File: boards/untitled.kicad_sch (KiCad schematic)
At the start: 20 parts, among them J11 RE12A, J12 RS485_airdata, Q3 NPN, U8 MAX3485, U9 MOUDLE-SEEEDUINO-XIAO-ESP32C3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

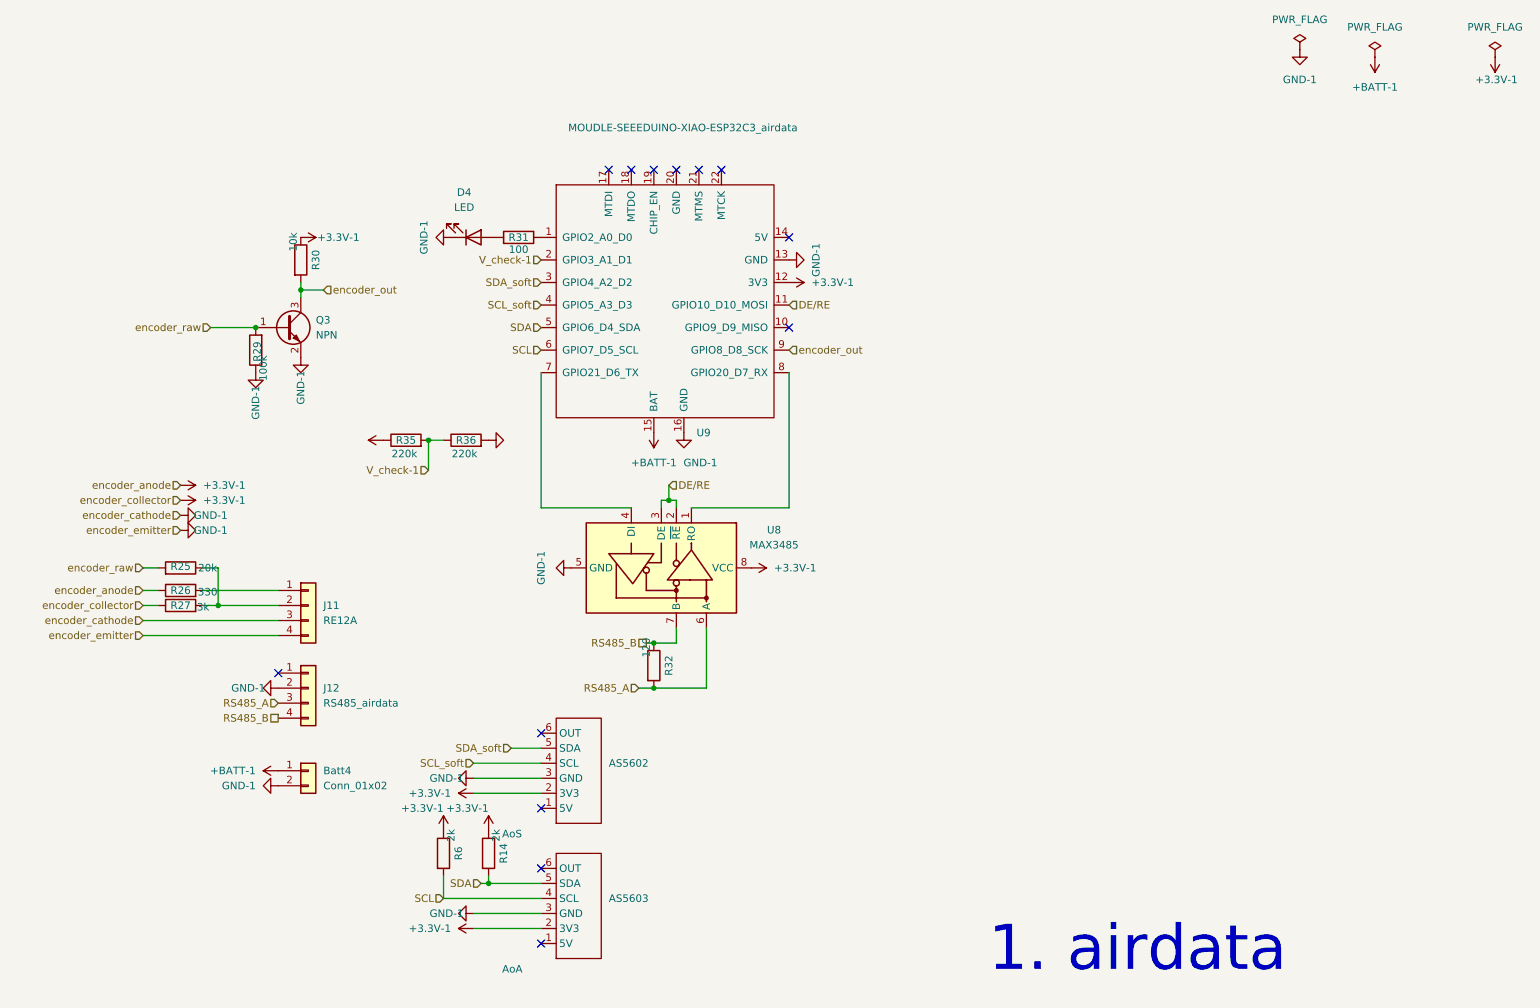
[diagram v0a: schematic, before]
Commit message: 増幅回路追加
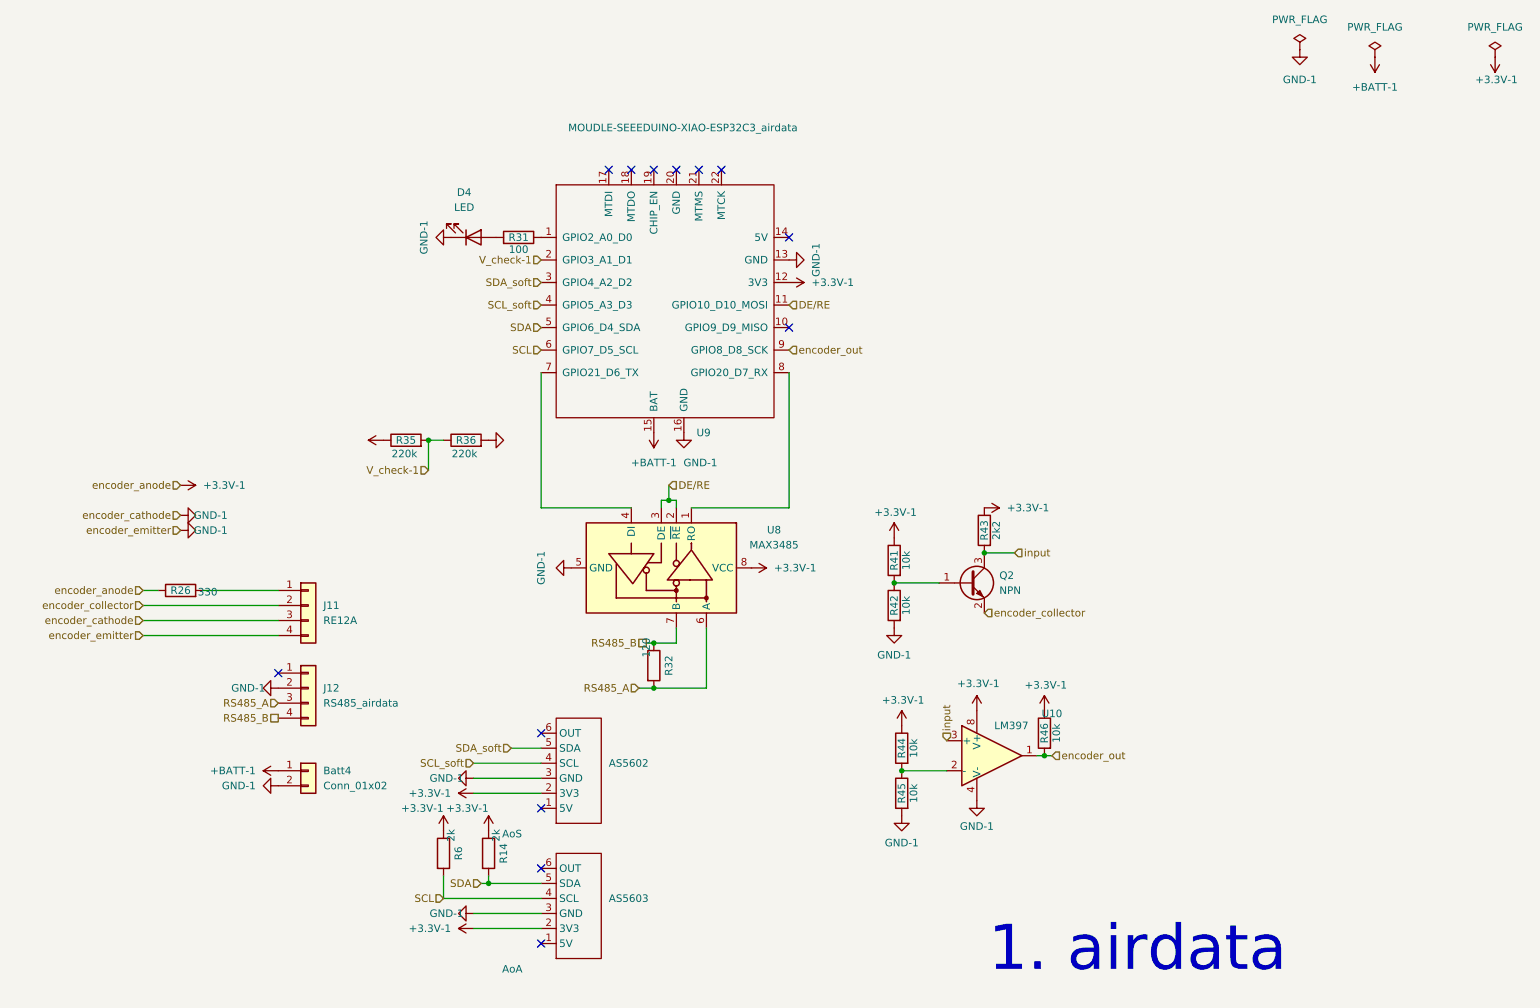
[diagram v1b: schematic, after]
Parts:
- removed Q3: NPN, Package_TO_SOT_SMD:SOT-23, symbol Transistor_BJT:MMBT2222A
- removed R25: 20k, Resistor_SMD:R_0603_1608Metric_Pad0.98x0.95mm_HandSolder, symbol Device:R
- removed R27: 3k, Resistor_SMD:R_0603_1608Metric_Pad0.98x0.95mm_HandSolder, symbol Device:R
- removed R29: 100k, Resistor_SMD:R_0603_1608Metric_Pad0.98x0.95mm_HandSolder, symbol Device:R
- removed R30: 10k, Resistor_SMD:R_0603_1608Metric_Pad0.98x0.95mm_HandSolder, symbol Device:R
- added Q2: NPN, Package_TO_SOT_SMD:SOT-23, symbol Transistor_BJT:MMBT2222A
- added R41, R42, R44, R45, R46: 10k, Resistor_SMD:R_0603_1608Metric_Pad0.98x0.95mm_HandSolder, symbol Device:R
- added R43: 2k2, Resistor_SMD:R_0603_1608Metric_Pad0.98x0.95mm_HandSolder, symbol Device:R
- added U10: LM397, Package_SO:SOP-8_3.9x4.9mm_P1.27mm, symbol Comparator:LM397
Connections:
- net +3.3V-1: now also R41.1, R43.1, R44.1, R46.1, U10.8 (V+)
- net GND-1: now also R42.2, R45.2, U10.4 (V-)
- net encoder_out: now also R46.2, U10.1
- net encoder_collector: now reaches J11.2 (Pin_2)
- net encoder_collector: now also Q2.2 (E)
- new net: Q2.1 (B), R41.2, R42.1
- new net: R44.2, R45.1, U10.2 (-)
- new net input: Q2.3 (C), R43.2, U10.3 (+)

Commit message: DRCエラー解消
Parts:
- R26: value 330 -> 150
- U10: value LM397 -> TJ393
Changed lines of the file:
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@@
 			)
 		)
-		(property "Value" "LM397"
+		(property "Value" "TJ393"
 			(at 189.992 135.89 0)
 			(effects
@@
 			)
 		)
-		(property "Value" "330"
+		(property "Value" "150"
 			(at 54.102 113.284 90)
 			(effects

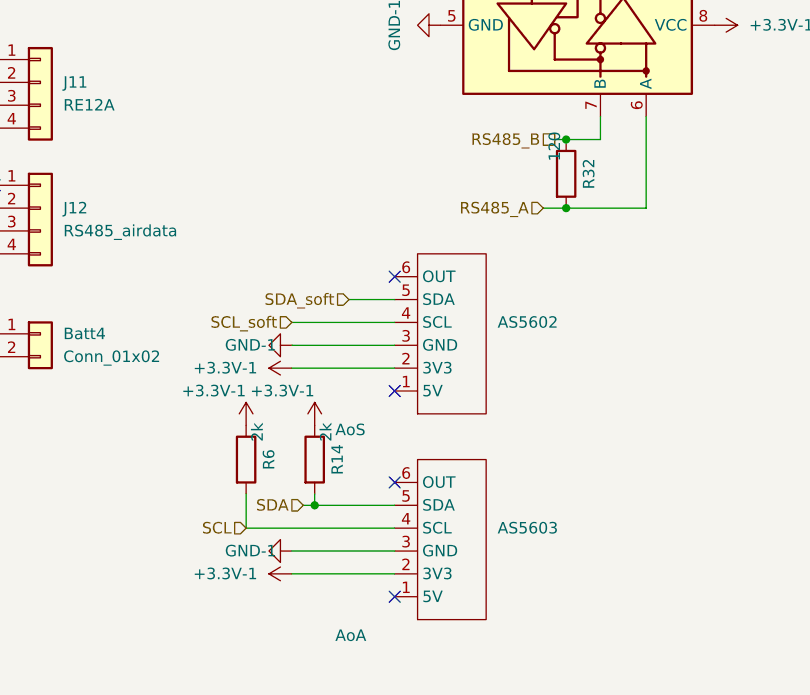
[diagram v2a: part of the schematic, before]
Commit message: 動作確認をもとに統合版コード修正
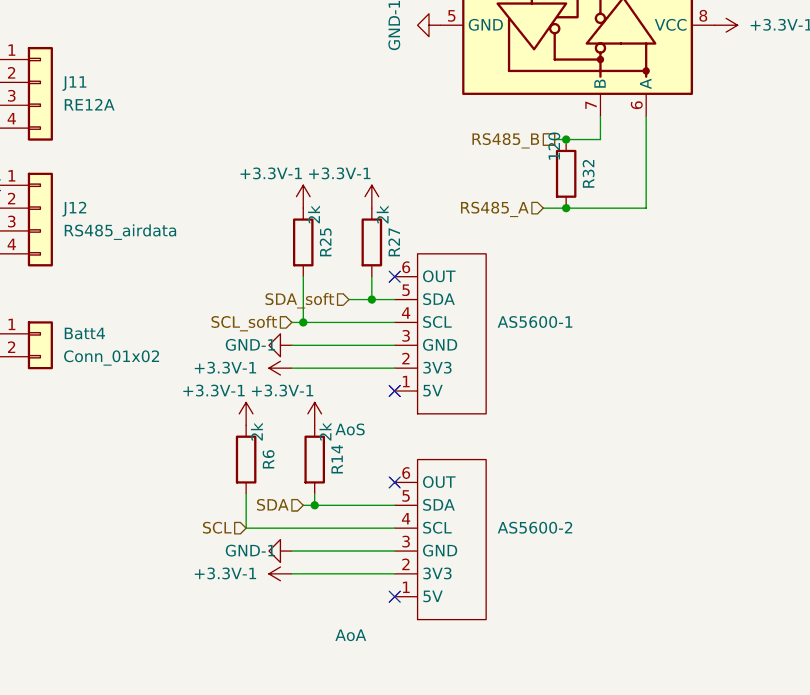
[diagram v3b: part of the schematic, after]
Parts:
- added R25, R27: 2k, Resistor_SMD:R_0603_1608Metric_Pad0.98x0.95mm_HandSolder, symbol Device:R
- renumbered AS5602 to AS5600-1, AS5603 to AS5600-2
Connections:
- net +3.3V-1: now also R25.1, R27.1
- net SCL_soft: now also R25.2
- net SDA_soft: now also R27.2
